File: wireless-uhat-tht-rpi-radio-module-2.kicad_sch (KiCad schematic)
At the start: 17 parts, among them J1 GPIO, J2 DEBUG, U1 CAT24C256_EP, U2 RMC20452

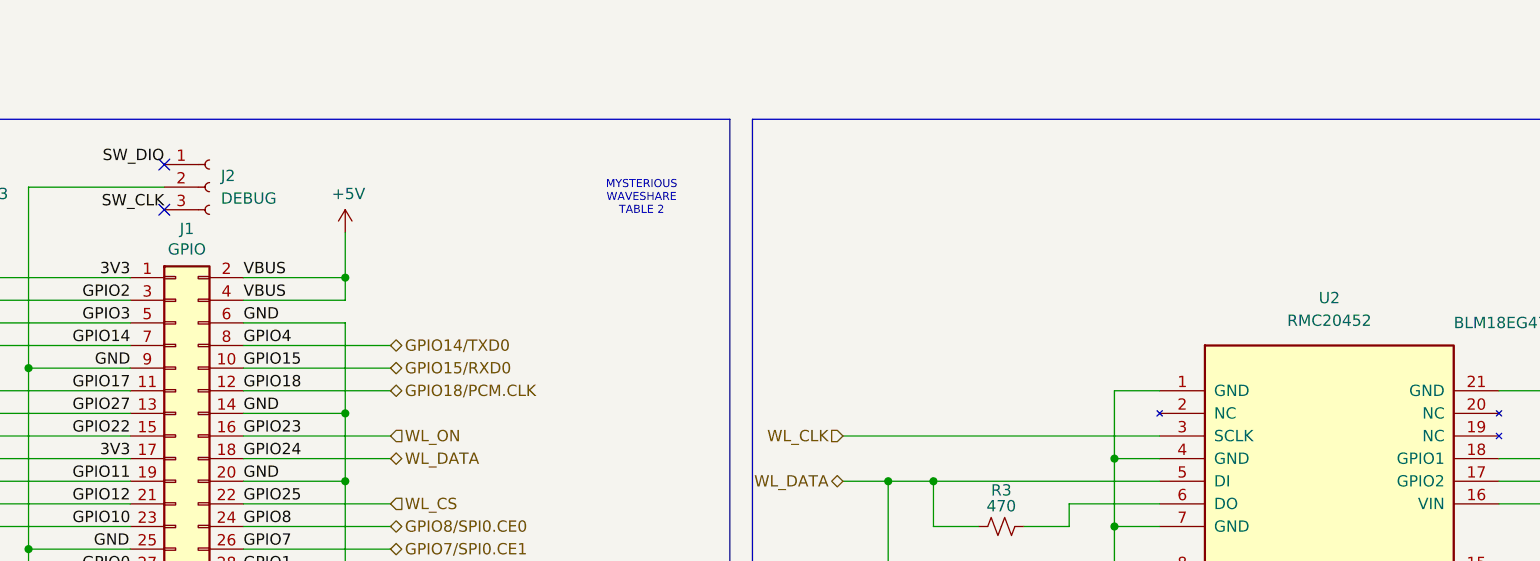
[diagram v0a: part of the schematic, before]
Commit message: tl;dr: make preparations to send board for prototyping
=======================================================================
added:
  misc/
      wireless-uhat-tht-rpi-radio-module-2.csv  - i don't remember where
        this is from

  gerbers/  - gerbers for board; used OSH guidelines for now
      wireless-uhat-tht-rpi-radio-module-2-B_Cu.gbl
      wireless-uhat-tht-rpi-radio-module-2-B_Mask.gbs
      wireless-uhat-tht-rpi-radio-module-2-B_Paste.gbp
      wireless-uhat-tht-rpi-radio-module-2-B_Silkscreen.gbo
      wireless-uhat-tht-rpi-radio-module-2-Edge_Cuts.gm1
      wireless-uhat-tht-rpi-radio-module-2-F_Cu.gtl
      wireless-uhat-tht-rpi-radio-module-2-F_Mask.gts
      wireless-uhat-tht-rpi-radio-module-2-F_Paste.gtp
      wireless-uhat-tht-rpi-radio-module-2-F_Silkscreen.gto
      wireless-uhat-tht-rpi-radio-module-2-NPTH-drl_map.gbr
      wireless-uhat-tht-rpi-radio-module-2-NPTH.drl
      wireless-uhat-tht-rpi-radio-module-2-PTH-drl_map.gbr
      wireless-uhat-tht-rpi-radio-module-2-PTH.drl
      wireless-uhat-tht-rpi-radio-module-2-job.gbrjob

  misc/img/ - images of board
      wireless-uhat-tht-rpi-radio-module-2_topside.png
      wireless-uhat-tht-rpi-radio-module-2_underside.png
      wireless-uhat-tht-rpi-radio-module-2_whateverside.png

-----------------------------------------------------------------------
removed:
  wireless-uhat-rpi-radio-module-2-backups/
      wireless-uhat-rpi-radio-module-2*.zip - renamed this board

  grb/
      *.txt - moved output location and changed output settings
-----------------------------------------------------------------------
modified:
  ./
      wireless-uhat-tht-rpi-radio-module-2.kicad_pcb - edited layout for
        manufacturer specs
      wireless-uhat-tht-rpi-radio-module-2.kicad_prl - i should untrack
        this, it's just the state / current view file
      wireless-uhat-tht-rpi-radio-module-2.kicad_pro - edited board
        constraints to to fit OSH guidelines / capabilities
      wireless-uhat-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
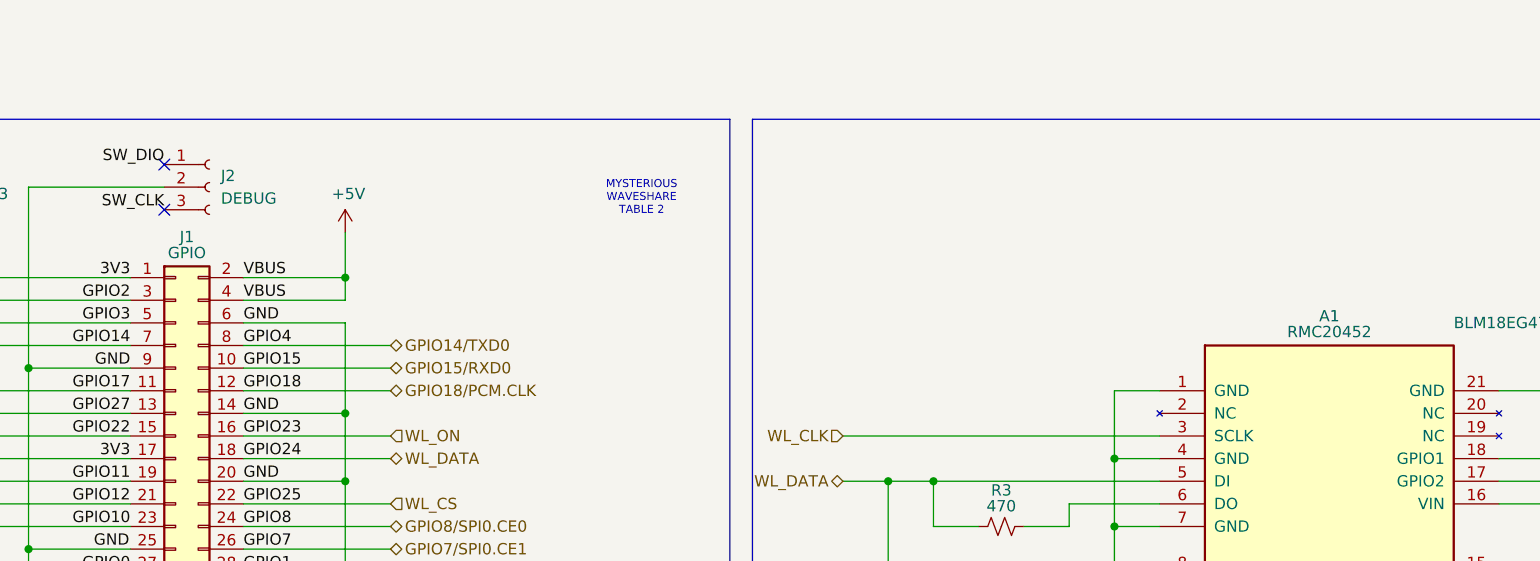
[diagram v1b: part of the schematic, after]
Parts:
- renumbered U2 to A1
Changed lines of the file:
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@@
 		(dnp no)
 		(property "Reference" "J1"
-			(at 83.82 55.4798 0)
+			(at 83.82 56.388 0)
 			(effects
 				(font
@@
 		)
 		(property "Value" "GPIO"
-			(at 83.82 57.785 0)
+			(at 83.82 58.1852 0)
 			(effects
 				(font
@@
 		(on_board yes)
 		(dnp no)
-		(property "Reference" "U2"
-			(at 212.09 63.246 0)
+		(property "Reference" "A1"
+			(at 212.09 65.278 0)
 			(effects
 				(font
@@
 		)
 		(property "Value" "RMC20452"
-			(at 212.09 65.786 0)
+			(at 212.09 67.056 0)
 			(effects
 				(font
@@
 			(project "wireless-uhat-rpi-radio-module-2"
 				(path "/e63e39d7-6ac0-4ffd-8aa3-1841a4541b55"
-					(reference "U2")
-					(unit 1)
-				)
+					(reference "A1")
+					(unit 1)
+				)

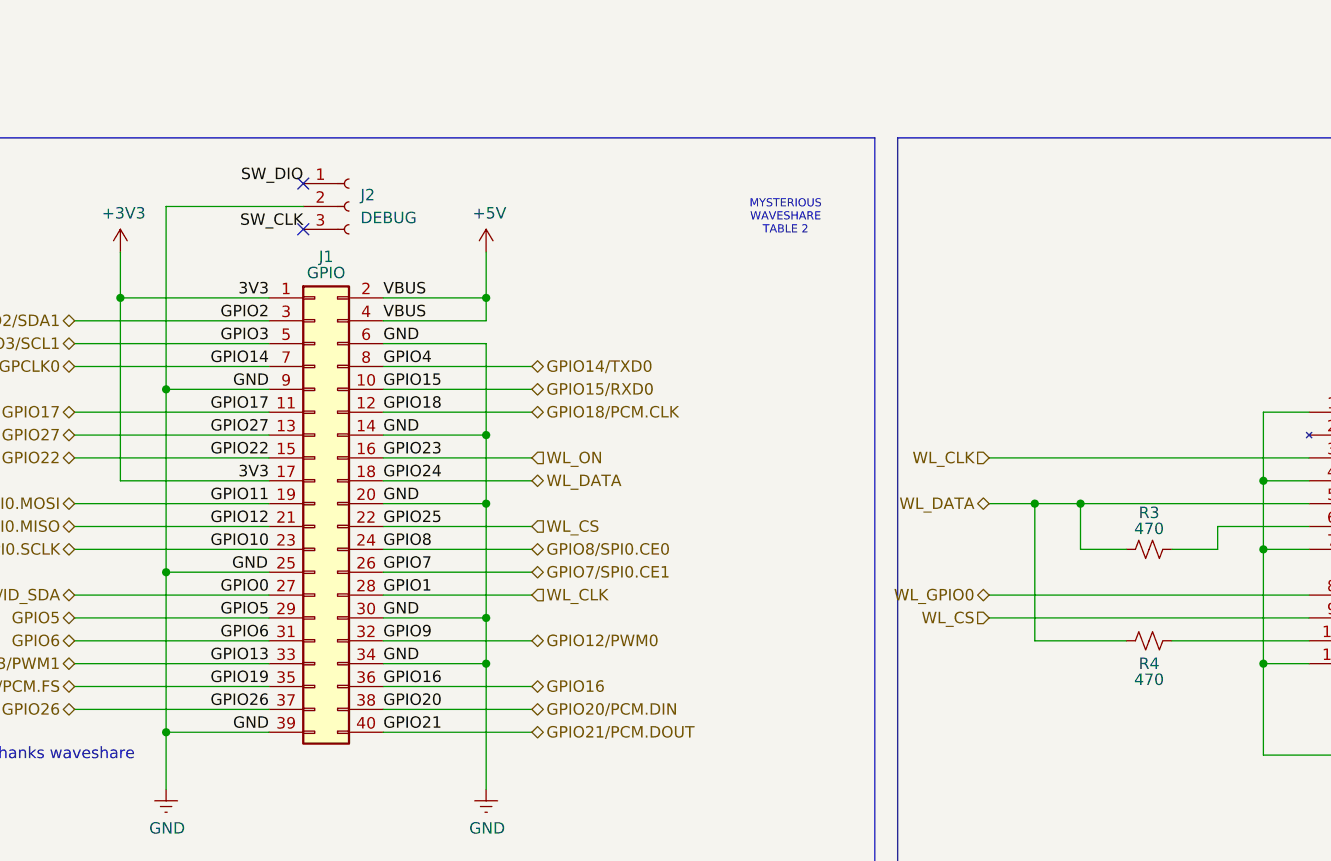
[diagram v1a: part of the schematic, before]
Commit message: tl;dr: finishing touches to send board in for prototyping
=======================================================================
added:
  gerbers/
      wireless-uhat-tht-rpi-radio-module-2.7z - forgot to remove before
        commit

-----------------------------------------------------------------------
modified:
  gerbers/  - regenerated to reflect updates
      wireless-uhat-tht-rpi-radio-module-2-B_Cu.gbl
      wireless-uhat-tht-rpi-radio-module-2-B_Mask.gbs
      wireless-uhat-tht-rpi-radio-module-2-B_Paste.gbp
      wireless-uhat-tht-rpi-radio-module-2-B_Silkscreen.gbo
      wireless-uhat-tht-rpi-radio-module-2-Edge_Cuts.gm1
      wireless-uhat-tht-rpi-radio-module-2-F_Cu.gtl
      wireless-uhat-tht-rpi-radio-module-2-F_Mask.gts
      wireless-uhat-tht-rpi-radio-module-2-F_Paste.gtp
      wireless-uhat-tht-rpi-radio-module-2-F_Silkscreen.gto
      wireless-uhat-tht-rpi-radio-module-2-NPTH-drl_map.gbr
      wireless-uhat-tht-rpi-radio-module-2-NPTH.drl
      wireless-uhat-tht-rpi-radio-module-2-PTH-drl_map.gbr
      wireless-uhat-tht-rpi-radio-module-2-PTH.drl
      wireless-uhat-tht-rpi-radio-module-2-job.gbrjob

  ./    - updated fonts, removed debug connector (will remove from
    mainboard if needed)
      wireless-uhat-tht-rpi-radio-module-2.kicad_pcb
      wireless-uhat-tht-rpi-radio-module-2.kicad_prl
      wireless-uhat-tht-rpi-radio-module-2.kicad_pro
      wireless-uhat-tht-rpi-radio-module-2.kicad_sch

-----------------------------------------------------------------------
renamed:
  misc/wireless-uhat-tht-rpi-radio-module-2.csv
      -> misc/wireless-uhat-tht-rpi-radio-module-2_BOM.csv
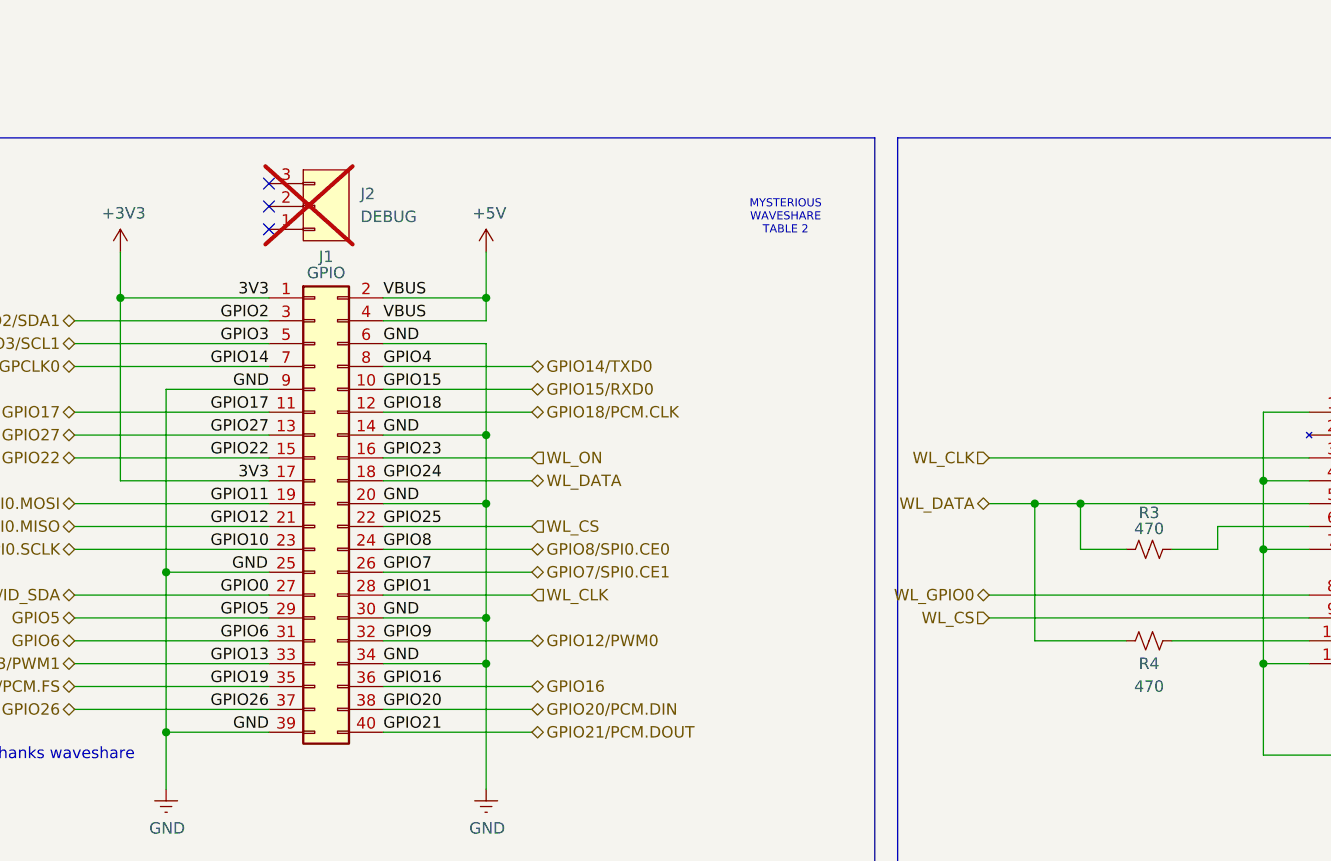
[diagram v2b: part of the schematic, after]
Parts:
- A1: now left out of the parts list
- J2: footprint Connector_PinSocket_2.54mm:PinSocket_1x03_P2.54mm_Vertical -> lsc-connector-board:BG12503A110440ND; symbol Connector:Conn_01x03_Socket -> connectors-board-added:BG125-03-A-1-1-0440-N-D; Height (none) -> 5.15; Manufacturer_Name (none) -> GCT (GLOBAL CONNECTOR TECHNOLOGY); Manufacturer_Part_Number (none) -> BG125-03-A-1-1-0440-N-D; Mouser Part Number (none) -> 640-BG12503A110440ND; Mouser Price/Stock (none) -> https://www.mouser.co.uk/ProductDetail/GCT/BG125-03-A-1-1-0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; now not fitted; now left out of the parts list
- L1: Part Number (none) -> BLM18EG471SN1D
- LED1: Part Number (none) -> 599-0060-007F
- LED2: Part Number (none) -> 599-0090-137F
- R3, R4, R8: Part Number (none) -> ERA-6AEB471V; part number ERA-6AEB471V -> (none)
- R5, R6: Part Number (none) -> ERA-6AEB103V; part number ERA-6AEB103V -> (none)
- R7: part number ERA-6AEB471V -> (none)
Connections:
- net EP: no longer J2.2 (Pin_2)
- net SW_CLK: no longer names the net of J2.3
- net SW_DIO: no longer names the net of J2.1
- no-connect marks 5 -> 6
